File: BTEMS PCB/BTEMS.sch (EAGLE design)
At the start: 22 parts

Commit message: Solidified part position, added BOM
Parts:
- ARDUINO_A4-5, ARDUINO_A6-7: device SparkFun-Connectors:M02LOCK -> SparkFun-Connectors:M02PTH
- BAT_HEADER: device SparkFun-Connectors:M023.5MM_LOCK -> SparkFun-Connectors:M022.54MM_SCREWTERM
- EXHEADER_A4-5, EXHEADER_A6-7: device SparkFun-Connectors:M02PTH -> SparkFun-Connectors:M02LOCK
- I2C_R1, I2C_R2: value (none) -> 2.2k
- RTC_HEADER: device SparkFun-Connectors:M04LOCK -> SparkFun-Connectors:M06FEMALE_LOCK
- renumbered U$1 to SDSLOT
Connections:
- net 3.3V: now also RTC_HEADER.2, RTC_HEADER.5
- net GND: now also RTC_HEADER.6
- net VCC: no longer RTC_HEADER.2
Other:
- moved on the sheet: BAT_HEADER, MLX_HEADER, S1, SHT_HEADER

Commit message: Routed board
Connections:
- removed net VCC: EXHEADER_A0-3.4
- new net RST2: ARDUINO_D2-9.3, EXHEADER_D2-9.3
- net 3.3V: now also EXHEADER_A0-3.4
- net BAT_IN: no longer R3.2
- net D10: now also SDSLOT.CS
- net D4: no longer SDSLOT.CS
- net RAW: now also R3.2
- net RST: no longer ARDUINO_D2-9.3, EXHEADER_D2-9.3
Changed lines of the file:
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@@
 <net name="RST" class="0">
-<segment>
-<pinref part="ARDUINO_D2-9" gate="G$1" pin="3"/>
-<wire x1="187.96" y1="172.72" x2="182.88" y2="172.72" width="0.1524" layer="91"/>
-<label x="182.88" y="172.72" size="1.778" layer="95"/>
-</segment>
 <segment>
 <pinref part="ARDUINO_A0-3" gate="G$1" pin="3"/>
 <wire x1="215.9" y1="172.72" x2="220.98" y2="172.72" width="0.1524" layer="91"/>
 <label x="215.9" y="172.72" size="1.778" layer="95"/>
-</segment>
-<segment>
-<pinref part="EXHEADER_D2-9" gate="G$1" pin="3"/>
-<wire x1="187.96" y1="134.62" x2="182.88" y2="134.62" width="0.1524" layer="91"/>
-<label x="182.88" y="134.62" size="1.778" layer="95"/>
 </segment>
 <segment>
@@
 <label x="182.88" y="124.46" size="1.778" layer="95"/>
 </segment>
-<segment>
-<pinref part="SDSLOT" gate="G$1" pin="CS"/>
-<wire x1="264.16" y1="147.32" x2="259.08" y2="147.32" width="0.1524" layer="91"/>
-<label x="259.08" y="147.32" size="1.778" layer="95"/>
-</segment>
 </net>
 <net name="D5" class="0">
@@
 <label x="157.48" y="104.14" size="1.778" layer="95"/>
 </segment>
-</net>
-<net name="VCC" class="0">
-<segment>
-<pinref part="EXHEADER_A0-3" gate="G$1" pin="4"/>
-<wire x1="215.9" y1="132.08" x2="220.98" y2="132.08" width="0.1524" layer="91"/>
-<label x="215.9" y="132.08" size="1.778" layer="95"/>
+<segment>
+<pinref part="R3" gate="G$1" pin="2"/>
+<wire x1="248.92" y1="215.9" x2="248.92" y2="220.98" width="0.1524" layer="91"/>
+<label x="248.92" y="215.9" size="1.778" layer="95" rot="R90"/>
 </segment>
 </net>
@@
 <wire x1="215.9" y1="111.76" x2="220.98" y2="111.76" width="0.1524" layer="91"/>
 <label x="215.9" y="111.76" size="1.778" layer="95"/>
+</segment>
+<segment>
+<pinref part="SDSLOT" gate="G$1" pin="CS"/>
+<wire x1="264.16" y1="147.32" x2="259.08" y2="147.32" width="0.1524" layer="91"/>
+<label x="259.08" y="147.32" size="1.778" layer="95"/>
 </segment>
 </net>
@@
 <label x="134.62" y="165.1" size="1.778" layer="95"/>
 </segment>
+<segment>
+<pinref part="EXHEADER_A0-3" gate="G$1" pin="4"/>
+<wire x1="215.9" y1="132.08" x2="220.98" y2="132.08" width="0.1524" layer="91"/>
+<label x="215.9" y="132.08" size="1.778" layer="95"/>
+</segment>
 </net>
 <net name="BAT_IN" class="0">
@@
 <label x="134.62" y="106.68" size="1.778" layer="95"/>
 </segment>
-<segment>
-<pinref part="R3" gate="G$1" pin="2"/>
-<wire x1="248.92" y1="215.9" x2="248.92" y2="220.98" width="0.1524" layer="91"/>
-<label x="248.92" y="215.9" size="1.778" layer="95" rot="R90"/>
-</segment>
 </net>
 <net name="N$2" class="0">
@@
 </segment>
 </net>
+<net name="RST2" class="0">
+<segment>
+<pinref part="ARDUINO_D2-9" gate="G$1" pin="3"/>
+<wire x1="187.96" y1="172.72" x2="182.88" y2="172.72" width="0.1524" layer="91"/>
+<label x="182.88" y="172.72" size="1.778" layer="95"/>
+</segment>
+<segment>
+<pinref part="EXHEADER_D2-9" gate="G$1" pin="3"/>
+<wire x1="187.96" y1="134.62" x2="182.88" y2="134.62" width="0.1524" layer="91"/>
+<label x="182.88" y="134.62" size="1.778" layer="95"/>
+</segment>
+</net>

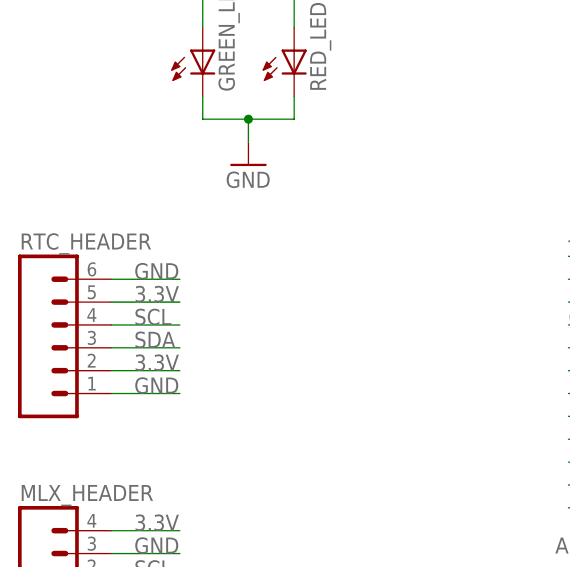
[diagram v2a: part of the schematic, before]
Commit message: Added silkscreen, BOM parts
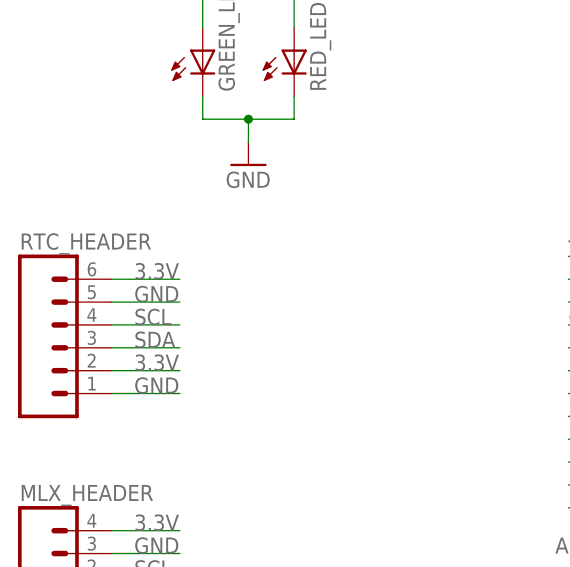
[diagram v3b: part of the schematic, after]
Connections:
- net 3.3V: now also RTC_HEADER.6; no longer RTC_HEADER.5
- net GND: now also RTC_HEADER.5; no longer RTC_HEADER.6
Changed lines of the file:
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@@
-</segment>
-<segment>
-<pinref part="RTC_HEADER" gate="G$1" pin="6"/>
-<wire x1="132.08" y1="175.26" x2="139.7" y2="175.26" width="0.1524" layer="91"/>
-<label x="134.62" y="175.26" size="1.778" layer="95"/>
 </segment>
 <segment>
@@
 <wire x1="132.08" y1="162.56" x2="139.7" y2="162.56" width="0.1524" layer="91"/>
 <label x="134.62" y="162.56" size="1.778" layer="95"/>
+</segment>
+<segment>
+<pinref part="RTC_HEADER" gate="G$1" pin="5"/>
+<wire x1="132.08" y1="172.72" x2="139.7" y2="172.72" width="0.1524" layer="91"/>
+<label x="134.62" y="172.72" size="1.778" layer="95"/>
 </segment>
 </net>
@@
 </segment>
 <segment>
-<pinref part="RTC_HEADER" gate="G$1" pin="5"/>
-<wire x1="132.08" y1="172.72" x2="139.7" y2="172.72" width="0.1524" layer="91"/>
-<label x="134.62" y="172.72" size="1.778" layer="95"/>
-</segment>
-<segment>
 <pinref part="RTC_HEADER" gate="G$1" pin="2"/>
 <wire x1="132.08" y1="165.1" x2="139.7" y2="165.1" width="0.1524" layer="91"/>
@@
 <label x="215.9" y="132.08" size="1.778" layer="95"/>
 </segment>
-</net>
+<segment>
+<pinref part="RTC_HEADER" gate="G$1" pin="6"/>
+<wire x1="132.08" y1="175.26" x2="139.7" y2="175.26" width="0.1524" layer="91"/>
+<label x="134.62" y="175.26" size="1.778" layer="95"/>
+</segment>
+</net>

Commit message: Many changes and added gerber files
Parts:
- R1: value 24k -> R1
- R2: value 30k -> R2
- R_GLED: value (none) -> 220
- R_RLED: value (none) -> 270
- renumbered R3 to R1, R4 to R2
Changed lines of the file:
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@@
 <part name="BAT_HEADER" library="SparkFun-Connectors" deviceset="M02" device="2.54MM_SCREWTERM"/>
 <part name="S1" library="SparkFun-Electromechanical" deviceset="SWITCH-SPDT" device="PTH"/>
-<part name="R3" library="adafruit" deviceset="R-US_" device="0207/7" value="24k"/>
-<part name="R4" library="adafruit" deviceset="R-US_" device="0207/7" value="30k"/>
+<part name="R1" library="adafruit" deviceset="R-US_" device="0207/7" value="R1"/>
+<part name="R2" library="adafruit" deviceset="R-US_" device="0207/7" value="R2"/>
 <part name="GND3" library="SparkFun-Aesthetics" deviceset="GND" device=""/>
 <part name="GREEN_LED" library="adafruit" deviceset="LED" device="3MM"/>
 <part name="RED_LED" library="adafruit" deviceset="LED" device="3MM"/>
-<part name="R_GLED" library="adafruit" deviceset="R-US_" device="0207/7"/>
-<part name="R_RLED" library="adafruit" deviceset="R-US_" device="0207/7"/>
+<part name="R_GLED" library="adafruit" deviceset="R-US_" device="0207/7" value="220"/>
+<part name="R_RLED" library="adafruit" deviceset="R-US_" device="0207/7" value="270"/>
 <part name="GND4" library="SparkFun-Aesthetics" deviceset="GND" device=""/>
 <part name="RTC_HEADER" library="SparkFun-Connectors" deviceset="M06" device="FEMALE_LOCK"/>
@@
 <instance part="BAT_HEADER" gate="G$1" x="124.46" y="104.14"/>
 <instance part="S1" gate="1" x="152.4" y="104.14" rot="R180"/>
-<instance part="R3" gate="G$1" x="248.92" y="210.82" rot="R90"/>
-<instance part="R4" gate="G$1" x="248.92" y="195.58" rot="R90"/>
+<instance part="R1" gate="G$1" x="248.92" y="210.82" rot="R90"/>
+<instance part="R2" gate="G$1" x="248.92" y="195.58" rot="R90"/>
 <instance part="GND3" gate="1" x="248.92" y="185.42"/>
 <instance part="GREEN_LED" gate="G$1" x="142.24" y="200.66"/>
@@
 </segment>
 <segment>
-<pinref part="R4" gate="G$1" pin="1"/>
+<pinref part="R2" gate="G$1" pin="1"/>
 <wire x1="248.92" y1="190.5" x2="248.92" y2="187.96" width="0.1524" layer="91"/>
 <pinref part="GND3" gate="1" pin="GND"/>
@@
 </segment>
 <segment>
-<pinref part="R3" gate="G$1" pin="2"/>
+<pinref part="R1" gate="G$1" pin="2"/>
 <wire x1="248.92" y1="215.9" x2="248.92" y2="220.98" width="0.1524" layer="91"/>
 <label x="248.92" y="215.9" size="1.778" layer="95" rot="R90"/>
@@
 </segment>
 <segment>
-<pinref part="R3" gate="G$1" pin="1"/>
-<pinref part="R4" gate="G$1" pin="2"/>
+<pinref part="R1" gate="G$1" pin="1"/>
+<pinref part="R2" gate="G$1" pin="2"/>
 <wire x1="248.92" y1="205.74" x2="248.92" y2="203.2" width="0.1524" layer="91"/>
 <wire x1="248.92" y1="203.2" x2="248.92" y2="200.66" width="0.1524" layer="91"/>

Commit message: v1.1 changes added
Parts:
- added EXHEADER_POW1: (no value), SparkFun-Connectors:M02PTH
- BAT_HEADER: device SparkFun-Connectors:M022.54MM_SCREWTERM -> SparkFun-Connectors:M023.5MM
- R1: value R1 -> 24k
- R2: value R2 -> 30k
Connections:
- net 3.3V: now also EXHEADER_POW1.2
- net GND: now also EXHEADER_POW1.1
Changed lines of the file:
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@@
 <part name="SHT_HEADER" library="SparkFun-Connectors" deviceset="M04" device="LOCK"/>
 <part name="GND2" library="SparkFun-Aesthetics" deviceset="GND" device=""/>
-<part name="BAT_HEADER" library="SparkFun-Connectors" deviceset="M02" device="2.54MM_SCREWTERM"/>
+<part name="BAT_HEADER" library="SparkFun-Connectors" deviceset="M02" device="3.5MM"/>
 <part name="S1" library="SparkFun-Electromechanical" deviceset="SWITCH-SPDT" device="PTH"/>
-<part name="R1" library="adafruit" deviceset="R-US_" device="0207/7" value="R1"/>
-<part name="R2" library="adafruit" deviceset="R-US_" device="0207/7" value="R2"/>
+<part name="R1" library="adafruit" deviceset="R-US_" device="0207/7" value="24k"/>
+<part name="R2" library="adafruit" deviceset="R-US_" device="0207/7" value="30k"/>
 <part name="GND3" library="SparkFun-Aesthetics" deviceset="GND" device=""/>
 <part name="GREEN_LED" library="adafruit" deviceset="LED" device="3MM"/>
@@
 <part name="GND4" library="SparkFun-Aesthetics" deviceset="GND" device=""/>
 <part name="RTC_HEADER" library="SparkFun-Connectors" deviceset="M06" device="FEMALE_LOCK"/>
+<part name="EXHEADER_POW1" library="SparkFun-Connectors" deviceset="M02" device="PTH"/>
 </parts>
 <sheets>
@@
 <instance part="GND4" gate="1" x="147.32" y="187.96"/>
 <instance part="RTC_HEADER" gate="G$1" x="127" y="167.64"/>
+<instance part="EXHEADER_POW1" gate="G$1" x="124.46" y="88.9"/>
 </instances>
 <busses>
@@
 <label x="134.62" y="172.72" size="1.778" layer="95"/>
 </segment>
+<segment>
+<pinref part="EXHEADER_POW1" gate="G$1" pin="1"/>
+<wire x1="132.08" y1="88.9" x2="139.7" y2="88.9" width="0.1524" layer="91"/>
+<label x="134.62" y="88.9" size="1.778" layer="95"/>
+</segment>
 </net>
 <net name="D2" class="0">
@@
 <label x="134.62" y="175.26" size="1.778" layer="95"/>
 </segment>
-</net>
+<segment>
+<pinref part="EXHEADER_POW1" gate="G$1" pin="2"/>
+<wire x1="132.08" y1="91.44" x2="139.7" y2="91.44" width="0.1524" layer="91"/>
+<label x="134.62" y="91.44" size="1.778" layer="95"/>
+</segment>
+</net>

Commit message: v1.1 final, mostly finished BOM
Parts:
- added EXHEADER2_A4_5: (no value), SparkFun-Connectors:M02PTH
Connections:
- net SCL: now also EXHEADER2_A4_5.2
- net SDA: now also EXHEADER2_A4_5.1
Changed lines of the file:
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@@
 <part name="RTC_HEADER" library="SparkFun-Connectors" deviceset="M06" device="FEMALE_LOCK"/>
 <part name="EXHEADER_POW1" library="SparkFun-Connectors" deviceset="M02" device="PTH"/>
+<part name="EXHEADER2_A4_5" library="SparkFun-Connectors" deviceset="M02" device="PTH"/>
 </parts>
 <sheets>
@@
 <instance part="RTC_HEADER" gate="G$1" x="127" y="167.64"/>
 <instance part="EXHEADER_POW1" gate="G$1" x="124.46" y="88.9"/>
+<instance part="EXHEADER2_A4_5" gate="G$1" x="124.46" y="73.66"/>
 </instances>
 <busses>
@@
 <label x="134.62" y="167.64" size="1.778" layer="95"/>
 </segment>
+<segment>
+<pinref part="EXHEADER2_A4_5" gate="G$1" pin="1"/>
+<wire x1="132.08" y1="73.66" x2="139.7" y2="73.66" width="0.1524" layer="91"/>
+<label x="134.62" y="73.66" size="1.778" layer="95"/>
+</segment>
 </net>
 <net name="SCL" class="0">
@@
 <label x="134.62" y="170.18" size="1.778" layer="95"/>
 </segment>
-</net>
+<segment>
+<pinref part="EXHEADER2_A4_5" gate="G$1" pin="2"/>
+<wire x1="132.08" y1="76.2" x2="139.7" y2="76.2" width="0.1524" layer="91"/>
+<label x="134.62" y="76.2" size="1.778" layer="95"/>
+</segment>
+</net>
